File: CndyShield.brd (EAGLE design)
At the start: 69.9 x 78.1 mm, 38 parts, among them U1 ARDUINOR3-BPLACE

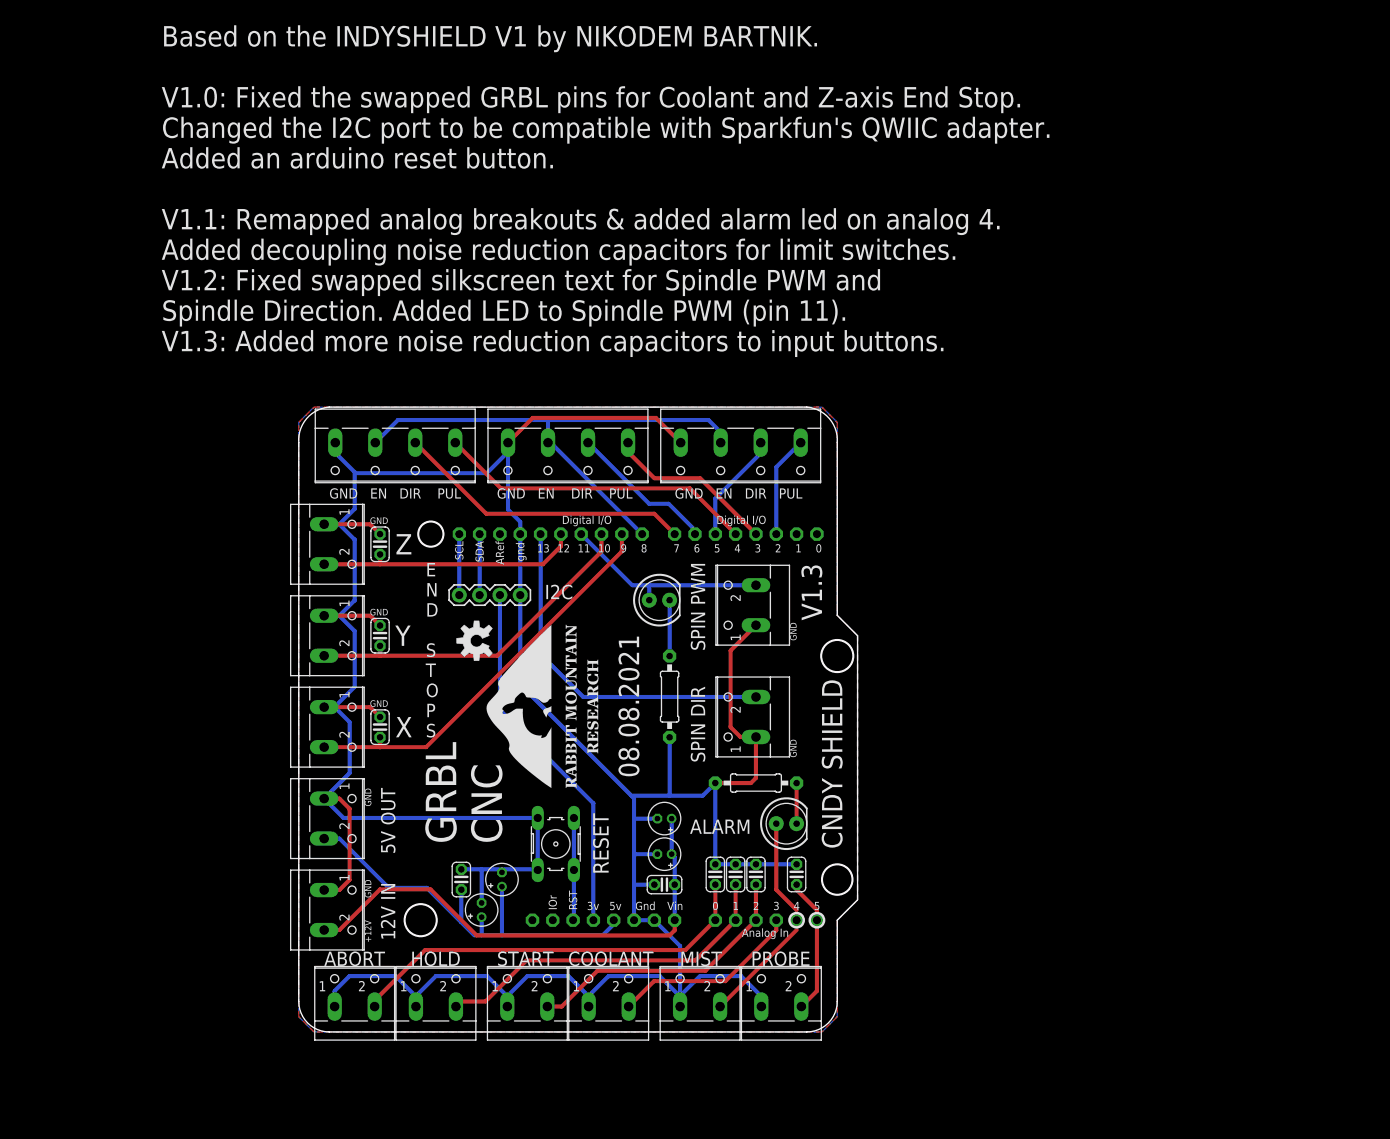
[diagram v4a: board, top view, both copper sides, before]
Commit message: Add files via upload
CN0DY Shield for GRBL V1.2. Ready for production. Fixed swapped silkscreen with spindle direction and spindle PWM. Added a number of new optional components. Added OSHW logo.
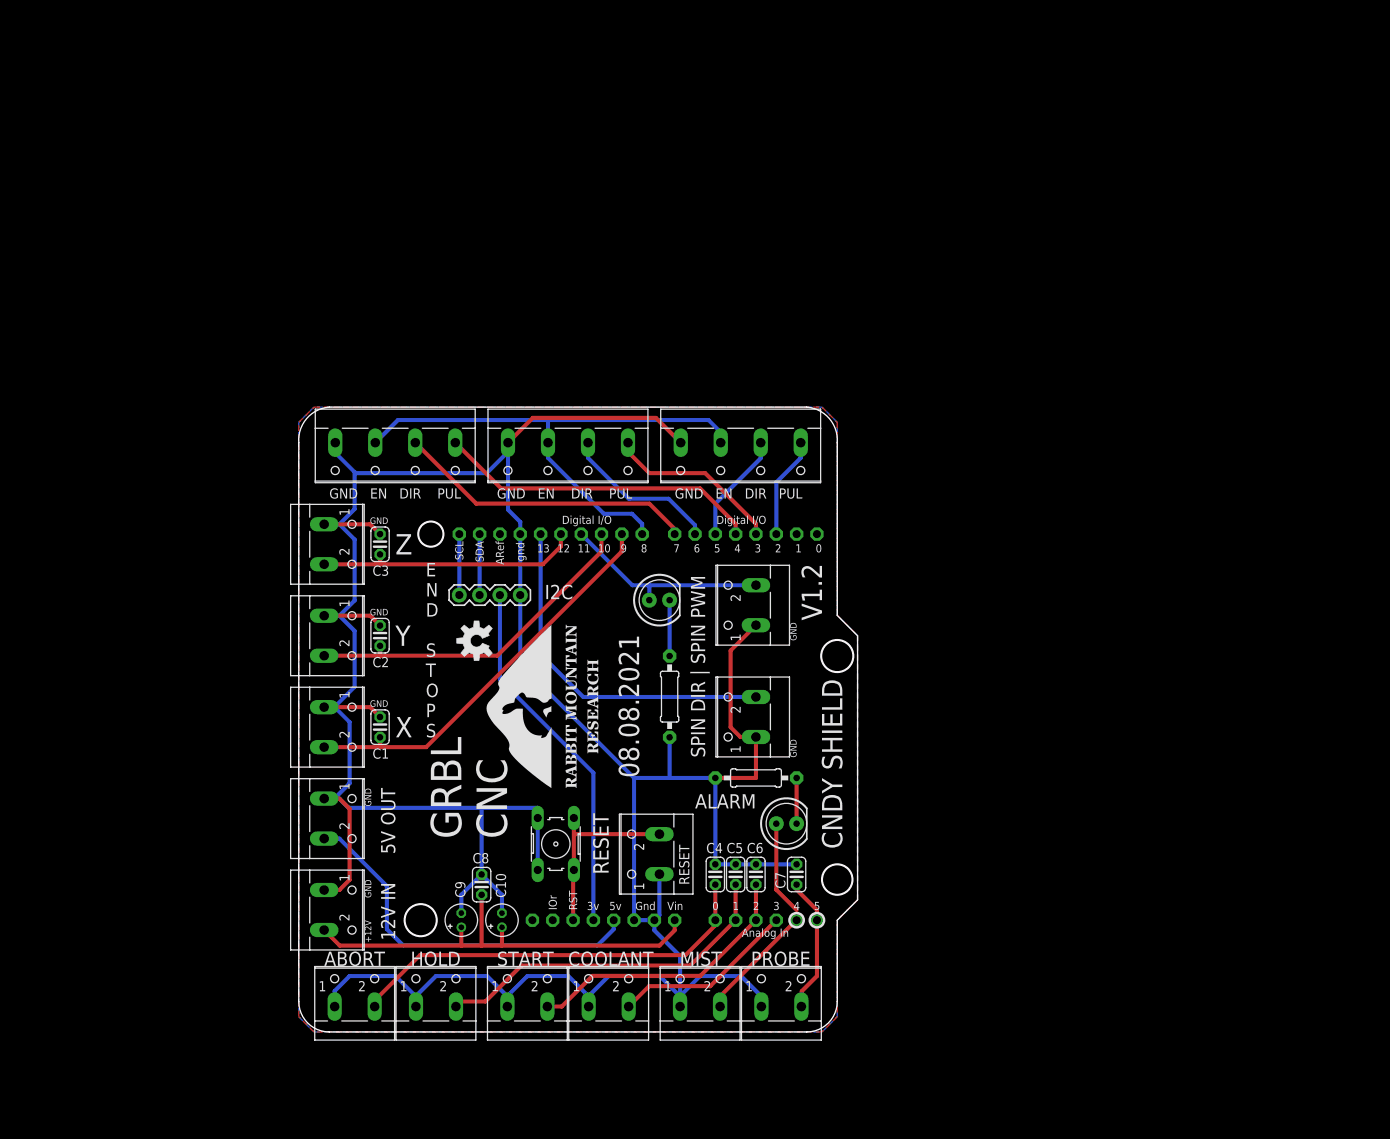
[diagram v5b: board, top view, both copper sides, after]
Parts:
- removed C11, C12, C13: (no value), adafruit:C025-024X044
- added RESET: (no value), con-wago-500:W237-102
- C10: device adafruit:C025-024X044 -> adafruit:E1,8-4
- C6, C7, C8: device adafruit:E1,8-4 -> adafruit:C025-024X044
- LOGO1: value (none) -> OSHW-LOGOM
- R1, R2: value 330 -> 150
- moved C7 36.8 mm to (97.8, 31.1)
- moved C5 34.3 mm to (90.2, 31.1)
- moved C10 27.3 mm to (61.0, 25.4)
- moved C8 24.3 mm to (58.4, 29.8), turned to 90 degrees
- moved C6 11.7 mm to (92.7, 31.1), turned to 90 degrees
- moved C4 6.48 mm to (87.6, 31.1), turned to 90 degrees
- moved C9 2.84 mm to (55.9, 25.4)
- moved R1 0.63 mm to (92.7, 43.2)
- renumbered U$1 to LOGO1
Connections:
- removed net N$7: S2.1, S2.2, U1.RESET
- new net RESET: RESET.2, S2.1, S2.2, U1.RESET
- net +12V: now also C10.+, C8.1, C9.+; no longer C4.1, C6.+, C8.+
- net +5V: no longer C5.1, C7.+, C9.+
- net ABORT: now also C4.1; no longer C10.1
- net GND: now also C10.-, C6.2, C7.2, C8.2, RESET.1; no longer C10.2, C11.2, C12.2, C13.2, C6.-, C7.-, C8.-
- net HOLD: now also C5.1; no longer C11.1
- net PROBE: now also C7.1; no longer C13.1
- net START: now also C6.1; no longer C12.1
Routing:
- net RESET: track 0.00 -> 23.5 mm
- net N$7: track 12.8 -> 0.00 mm
- net +5V: track 54.7 -> 46.8 mm
- net +12V: track 62.7 -> 57.6 mm
- net GND: track 423.0 -> 425.2 mm
- net S_EN: track 65.6 -> 67.5 mm
- net N$3: track 18.4 -> 19.9 mm
- net N$6: track 39.8 -> 40.5 mm
- net N$4: track 21.4 -> 22.1 mm
- net COOL: track 23.7 -> 22.9 mm
- net N$8: track 5.08 -> 5.71 mm
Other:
- board text added: "Based on the INDYSHIELD V1 by NIKODEM BARTNIK. V1.0: Fixed the swapped GRBL pins for Coolant and Z-axis End Stop. Changed the I2C port to be compatible with Sparkfun's QWIIC adapter. Added an arduino reset button. V1.1: Remapped analog breakouts & added alarm led on analog 4.Added decoupling noise reduction capacitors for limit switches. V1.2: Fixed swapped silkscreen text for Spindle PWM and Spi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"
- board text added: "SPIN DIR | SPIN PWM"
- board text added: "V1.2"
- board text removed: "Based on the INDYSHIELD V1 by NIKODEM BARTNIK. V1.0: Fixed the swapped GRBL pins for Coolant and Z-axis End Stop. Changed the I2C port to be compatible with Sparkfun's QWIIC adapter. Added an arduino reset button. V1.1: Remapped analog breakouts & added alarm led on analog 4. Added decoupling noise reduction capacitors for limit switches. V1.2: Fixed swapped silkscreen text for Spindle PWM and Sp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"
- board text removed: "SPIN DIR"
- board text removed: "SPIN PWM"
- board text removed: "V1.3"

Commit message: Add files via upload
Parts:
- moved R2 1.27 mm to (80.6, 53.3)
- moved D2 1.27 mm to (79.4, 65.4)
- moved X 0.64 mm to (90.2, 83.8)
- moved Y 0.64 mm to (68.6, 83.8)
- moved Z 0.63 mm to (47.0, 83.8)
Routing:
- net SPIN_E: track 26.4 -> 27.1 mm
- net N$6: track 40.5 -> 41.2 mm
- net N$5: track 37.5 -> 38.2 mm
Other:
- board size 69.9 x 78.1 mm -> 71.1 x 79.4 mm
- board text added: "---SPINDLE---"
- board text added: "--COOLANT--"
- board text added: "DIRECTION PWM"
- board text added: "FLOOD"
- board text removed: "COOLANT"
- board text removed: "SPIN DIR | SPIN PWM"

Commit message: Add files via upload
Fixed unrouted air wires. fixed 3.2mm mounting holes.
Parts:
- removed LIGHT: (no value), con-wago-500:W237-102
- added MIST: (no value), con-wago-500:W237-102
- moved C7 35.4 mm to (63.8, 21.1)
- moved PROBE 35.4 mm to (61.9, 5.88)
- moved U$2 35.4 mm to (39.0, 31.9)
- moved 5V 35.4 mm to (6.00, 28.1)
- moved ABORT 35.4 mm to (8.54, 5.88)
- moved C1 35.4 mm to (11.7, 39.5)
- moved C10 35.4 mm to (27.0, 15.4)
- moved C2 35.4 mm to (11.7, 51.0)
- moved C3 35.4 mm to (11.7, 62.4)
- moved C5 35.4 mm to (56.2, 21.1)
- moved C8 35.4 mm to (24.4, 19.8)
- moved C9 35.4 mm to (21.9, 15.4)
- moved COOL 35.4 mm to (40.3, 5.88)
- moved D2 35.4 mm to (45.4, 55.4)
- moved HOLD 35.4 mm to (18.7, 5.88)
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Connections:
- removed net LIGHT: LIGHT.2
- net GND: now also MIST.1; no longer LIGHT.1
- net MIST: now also MIST.2
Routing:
- net MIST: track 11.8 -> 27.9 mm
- net LIGHT: track 13.9 -> 0.00 mm
- net HOLD: track 44.2 -> 44.9 mm
- net S_EN: track 67.5 -> 68.1 mm
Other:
- outline, holes or cut-outs redrawn
- board text added: "08.13.2021"
- board text added: "Based on the INDYSHIELD V1 by NIKODEM BARTNIK. V1.0: Fixed the swapped GRBL pins for Coolant and Z-axis End Stop. Changed the I2C port to be compatible with Sparkfun's QWIIC adapter. Added an arduino reset button. V1.1: Remapped analog breakouts & added alarm led on analog 4. Added decoupling noise reduction capacitors for limit switches. V1.2: Fixed swapped silkscreen text for Spindle PWM and Sp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"
- board text removed: "08.08.2021"
- board text removed: "Based on the INDYSHIELD V1 by NIKODEM BARTNIK. V1.0: Fixed the swapped GRBL pins for Coolant and Z-axis End Stop. Changed the I2C port to be compatible with Sparkfun's QWIIC adapter. Added an arduino reset button. V1.1: Remapped analog breakouts & added alarm led on analog 4.Added decoupling noise reduction capacitors for limit switches. V1.2: Fixed swapped silkscreen text for Spindle PWM and Spi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"
